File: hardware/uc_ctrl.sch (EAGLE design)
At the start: 32 parts, among them Q4 si2305cd, Q7 si2305cd, T1 BC846, T3 BC846, Y1 32768Hz CFPX-217 12.5pF

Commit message: add pcb
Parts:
- removed C3: 100nF, rcl:C-EUC0805
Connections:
- net N$4 renamed UC_POW
- net 3V_CELL: now also U$9.2; no longer U$9.1
- net GND: no longer C3.1
- net PUSH: now also U$9.1; no longer U$9.2
- net UC_EN: now also U$1.18; no longer U$1.19
- net VCC: no longer C3.2
- net VCC_EN: now also U$1.19; no longer U$1.18
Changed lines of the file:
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@@
 <part name="GND4" library="SparkFun" deviceset="GND" device=""/>
 <part name="GND5" library="SparkFun" deviceset="GND" device=""/>
-<part name="C3" library="rcl" deviceset="C-EU" device="C0805" value="100nF"/>
-<part name="GND6" library="SparkFun" deviceset="GND" device=""/>
 </parts>
 <sheets>
@@
 <instance part="U$5" gate="G$1" x="121.92" y="33.02"/>
 <instance part="SUPPLY1" gate="G$1" x="78.74" y="127"/>
-<instance part="U$9" gate="G$1" x="50.8" y="124.46" rot="R90"/>
+<instance part="U$9" gate="G$1" x="48.26" y="124.46" rot="MR90"/>
 <instance part="D2" gate="G$1" x="71.12" y="119.38"/>
 <instance part="C2" gate="G$1" x="63.5" y="86.36"/>
@@
 <instance part="GND4" gate="1" x="73.66" y="35.56"/>
 <instance part="GND5" gate="1" x="116.84" y="22.86"/>
-<instance part="C3" gate="G$1" x="254" y="121.92" rot="R180"/>
-<instance part="GND6" gate="1" x="254" y="114.3"/>
 </instances>
 <busses>
@@
 </segment>
 <segment>
-<pinref part="C3" gate="G$1" pin="1"/>
-<pinref part="GND6" gate="1" pin="GND"/>
-<wire x1="254" y1="119.38" x2="254" y2="116.84" width="0.1524" layer="91"/>
-</segment>
-<segment>
 <pinref part="C11" gate="G$1" pin="2"/>
 <wire x1="218.44" y1="119.38" x2="220.98" y2="119.38" width="0.1524" layer="91"/>
@@
 <wire x1="269.24" y1="127" x2="269.24" y2="129.54" width="0.1524" layer="91"/>
 <wire x1="269.24" y1="129.54" x2="261.62" y2="129.54" width="0.1524" layer="91"/>
-<pinref part="C3" gate="G$1" pin="2"/>
-<wire x1="261.62" y1="129.54" x2="254" y2="129.54" width="0.1524" layer="91"/>
-<wire x1="254" y1="129.54" x2="254" y2="127" width="0.1524" layer="91"/>
 </segment>
 <segment>
@@
 <net name="UC_EN" class="0">
 <segment>
-<pinref part="U$1" gate="G$1" pin="19"/>
-<wire x1="149.86" y1="86.36" x2="157.48" y2="86.36" width="0.1524" layer="91"/>
-<label x="144.78" y="86.36" size="1.778" layer="95"/>
-</segment>
-<segment>
 <pinref part="R16" gate="G$1" pin="2"/>
 <wire x1="17.78" y1="25.4" x2="22.86" y2="25.4" width="0.1524" layer="91"/>
 <label x="12.7" y="27.94" size="1.778" layer="95"/>
 </segment>
-</net>
-<net name="N$4" class="0">
+<segment>
+<pinref part="U$1" gate="G$1" pin="18"/>
+<wire x1="157.48" y1="88.9" x2="149.86" y2="88.9" width="0.1524" layer="91"/>
+<label x="147.32" y="88.9" size="1.778" layer="95"/>
+</segment>
+</net>
+<net name="UC_POW" class="0">
 <segment>
 <pinref part="Q4" gate="G$1" pin="D"/>
@@
 <wire x1="38.1" y1="106.68" x2="38.1" y2="119.38" width="0.1524" layer="91"/>
 <pinref part="U$8" gate="G$1" pin="3V_CELL"/>
-<pinref part="U$9" gate="G$1" pin="1"/>
 <wire x1="38.1" y1="119.38" x2="38.1" y2="124.46" width="0.1524" layer="91"/>
 <wire x1="38.1" y1="119.38" x2="48.26" y2="119.38" width="0.1524" layer="91"/>
+<junction x="38.1" y="119.38"/>
+<pinref part="U$9" gate="G$1" pin="2"/>
 <wire x1="48.26" y1="119.38" x2="48.26" y2="124.46" width="0.1524" layer="91"/>
-<junction x="38.1" y="119.38"/>
 </segment>
 <segment>
@@
 <net name="VCC_EN" class="0">
 <segment>
-<pinref part="U$1" gate="G$1" pin="18"/>
-<wire x1="149.86" y1="88.9" x2="157.48" y2="88.9" width="0.1524" layer="91"/>
-<label x="144.78" y="88.9" size="1.778" layer="95"/>
-</segment>
-<segment>
 <pinref part="R20" gate="G$1" pin="2"/>
 <wire x1="20.32" y1="83.82" x2="12.7" y2="83.82" width="0.1524" layer="91"/>
 <label x="7.62" y="86.36" size="1.778" layer="95"/>
 </segment>
+<segment>
+<pinref part="U$1" gate="G$1" pin="19"/>
+<wire x1="157.48" y1="86.36" x2="149.86" y2="86.36" width="0.1524" layer="91"/>
+<label x="147.32" y="86.36" size="1.778" layer="95"/>
+</segment>
 </net>
 <net name="PUSH" class="0">
 <segment>
-<pinref part="U$9" gate="G$1" pin="2"/>
-<wire x1="50.8" y1="124.46" x2="50.8" y2="119.38" width="0.1524" layer="91"/>
 <pinref part="D2" gate="G$1" pin="A"/>
 <wire x1="50.8" y1="119.38" x2="63.5" y2="119.38" width="0.1524" layer="91"/>
@@
 <wire x1="68.58" y1="93.98" x2="63.5" y2="93.98" width="0.1524" layer="91"/>
 <junction x="63.5" y="93.98"/>
-</segment>
-</net>
+<pinref part="U$9" gate="G$1" pin="1"/>
+<wire x1="50.8" y1="119.38" x2="50.8" y2="124.46" width="0.1524" layer="91"/>
+</segment>
+</net>

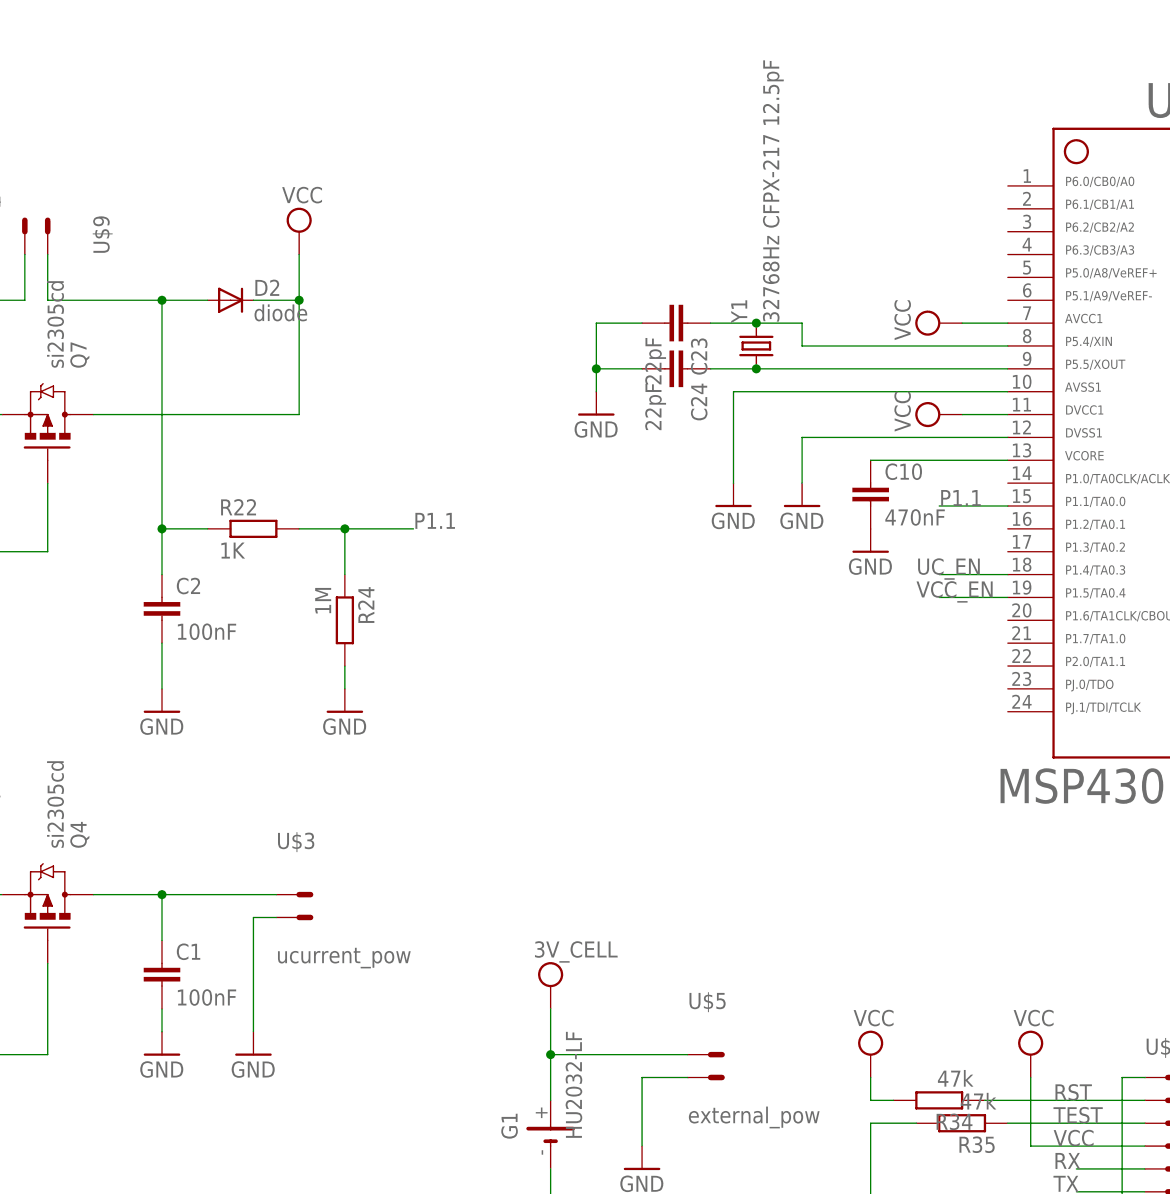
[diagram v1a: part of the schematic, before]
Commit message: also read uCurrent output voltage
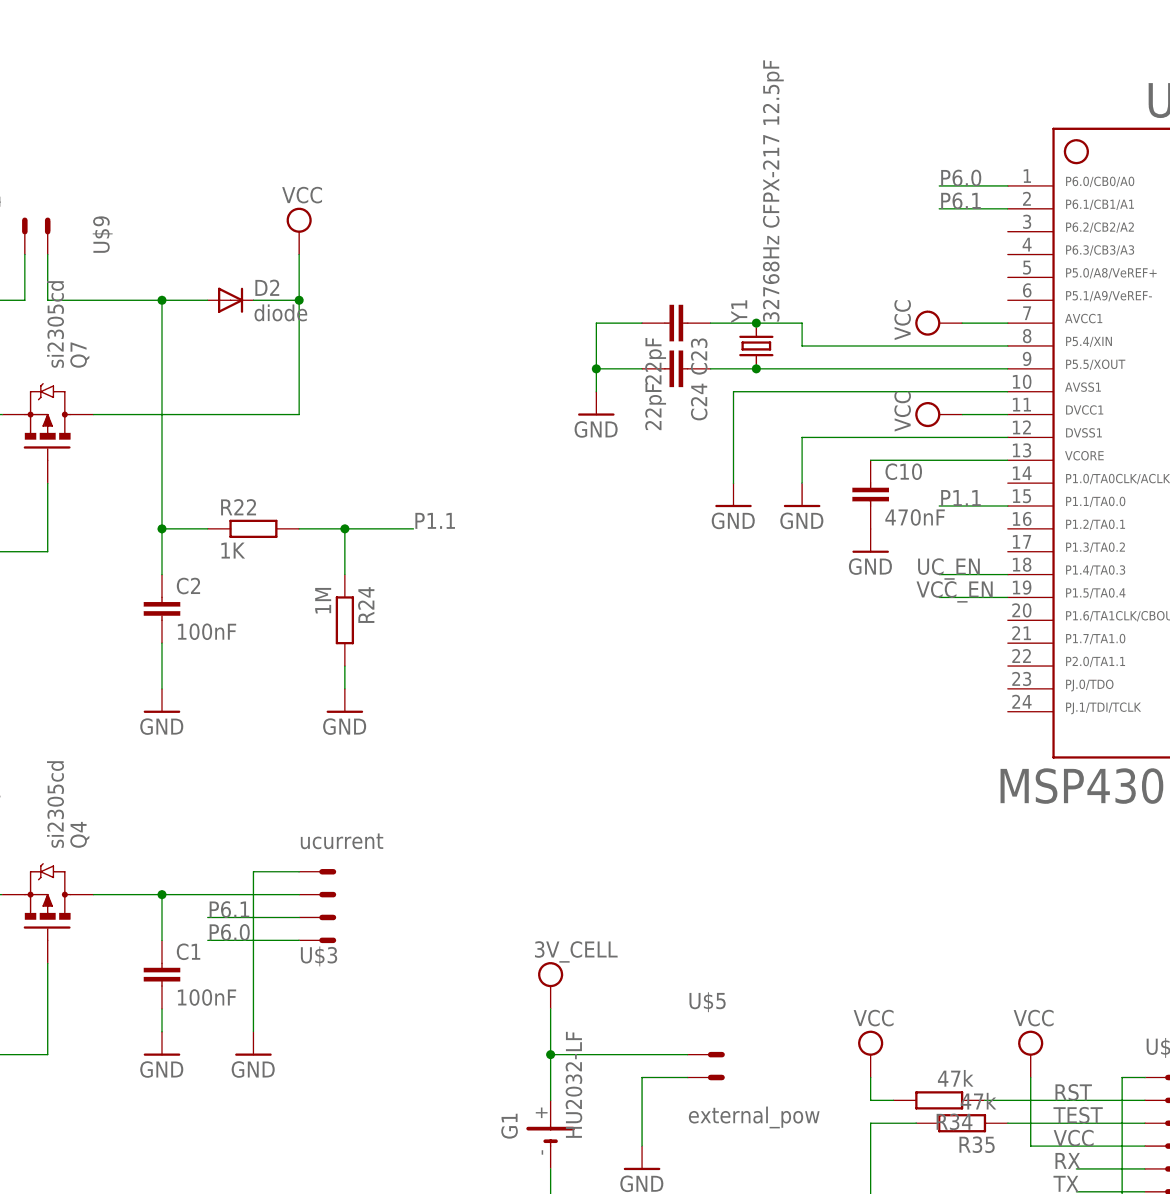
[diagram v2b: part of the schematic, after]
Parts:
- U$3: value ucurrent_pow -> ucurrent; device Simplex-Connectors:MOLEX_2VERTICAL -> Simplex-Connectors:MOLEX_4VERTICAL
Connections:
- new net P6.0: U$1.1, U$3.4
- new net P6.1: U$1.2, U$3.3
- net GND: now also U$3.1; no longer U$3.2
- net UC_POW: now also U$3.2; no longer U$3.1
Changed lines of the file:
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@@
 <part name="U$6" library="Simplex-Power" deviceset="3V_CELL" device=""/>
 <part name="U$8" library="Simplex-Power" deviceset="3V_CELL" device=""/>
-<part name="U$3" library="Simplex-Connectors" deviceset="MOLEX_2" device="VERTICAL" value="ucurrent_pow"/>
 <part name="U$5" library="Simplex-Connectors" deviceset="MOLEX_2" device="VERTICAL" value="external_pow"/>
 <part name="SUPPLY1" library="supply2" deviceset="VCC" device=""/>
@@
 <part name="GND4" library="SparkFun" deviceset="GND" device=""/>
 <part name="GND5" library="SparkFun" deviceset="GND" device=""/>
+<part name="U$3" library="Simplex-Connectors" deviceset="MOLEX_4" device="VERTICAL" value="ucurrent"/>
 </parts>
 <sheets>
@@
 <instance part="U$6" gate="G$1" x="106.68" y="40.64"/>
 <instance part="U$8" gate="G$1" x="38.1" y="124.46"/>
-<instance part="U$3" gate="G$1" x="76.2" y="50.8"/>
 <instance part="U$5" gate="G$1" x="121.92" y="33.02"/>
 <instance part="SUPPLY1" gate="G$1" x="78.74" y="127"/>
@@
 <instance part="GND4" gate="1" x="73.66" y="35.56"/>
 <instance part="GND5" gate="1" x="116.84" y="22.86"/>
+<instance part="U$3" gate="G$1" x="78.74" y="48.26"/>
 </instances>
 <busses>
@@
 </segment>
 <segment>
-<pinref part="U$3" gate="G$1" pin="2"/>
-<wire x1="76.2" y1="50.8" x2="73.66" y2="50.8" width="0.1524" layer="91"/>
-<wire x1="73.66" y1="50.8" x2="73.66" y2="38.1" width="0.1524" layer="91"/>
+<wire x1="73.66" y1="55.88" x2="73.66" y2="38.1" width="0.1524" layer="91"/>
 <pinref part="GND4" gate="1" pin="GND"/>
+<pinref part="U$3" gate="G$1" pin="1"/>
+<wire x1="73.66" y1="55.88" x2="78.74" y2="55.88" width="0.1524" layer="91"/>
 </segment>
 <segment>
@@
 <pinref part="C1" gate="G$1" pin="1"/>
 <wire x1="63.5" y1="53.34" x2="63.5" y2="48.26" width="0.1524" layer="91"/>
-<wire x1="63.5" y1="53.34" x2="76.2" y2="53.34" width="0.1524" layer="91"/>
-<pinref part="U$3" gate="G$1" pin="1"/>
+<wire x1="63.5" y1="53.34" x2="78.74" y2="53.34" width="0.1524" layer="91"/>
 <junction x="63.5" y="53.34"/>
+<pinref part="U$3" gate="G$1" pin="2"/>
 </segment>
 </net>
@@
 </segment>
 </net>
+<net name="P6.1" class="0">
+<segment>
+<pinref part="U$1" gate="G$1" pin="2"/>
+<wire x1="157.48" y1="129.54" x2="149.86" y2="129.54" width="0.1524" layer="91"/>
+<label x="149.86" y="129.54" size="1.778" layer="95"/>
+</segment>
+<segment>
+<pinref part="U$3" gate="G$1" pin="3"/>
+<wire x1="78.74" y1="50.8" x2="68.58" y2="50.8" width="0.1524" layer="91"/>
+<label x="68.58" y="50.8" size="1.778" layer="95"/>
+</segment>
+</net>
+<net name="P6.0" class="0">
+<segment>
+<pinref part="U$1" gate="G$1" pin="1"/>
+<wire x1="157.48" y1="132.08" x2="149.86" y2="132.08" width="0.1524" layer="91"/>
+<label x="149.86" y="132.08" size="1.778" layer="95"/>
+</segment>
+<segment>
+<pinref part="U$3" gate="G$1" pin="4"/>
+<wire x1="78.74" y1="48.26" x2="68.58" y2="48.26" width="0.1524" layer="91"/>
+<label x="68.58" y="48.26" size="1.778" layer="95"/>
+</segment>
+</net>

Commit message: rev 2
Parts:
- removed G1: HU2032-LF, Simplex-Battery:HU2032-LF
- removed U$9: push_button, Simplex-Connectors:MOLEX_2VERTICAL
- added C3, C4, C7: 100nF, rcl:C-EUC0805
- added C5, C6: 10uF, rcl:C-EUC0805
- added LED2: green, led:LEDCHIPLED_0805
- added R2: 100k, rcl:R-EU_R0805W
- added SJ1: (no value), SparkFun-Passives:SOLDERJUMPER_2WAYPASTE1&2
- added SJ2: SOLDERJUMPERNC2, SparkFun-Passives:SOLDERJUMPERNC2
- added U$4: SPST_TACTILE_SW, Simplex-Switches:SPST_TACTILE_SW
- added U$6: MOLEX_2HORIZONTAL, Simplex-Connectors:MOLEX_2HORIZONTAL
- added U1: 3vLDO, SparkFun-PowerIC:V_REG_LDOSMD
- U$2: device Simplex-Connectors:MOLEX_6VERTICAL -> Simplex-Connectors:MOLEX_6HORIZONTAL
- U$3: value ucurrent -> MOLEX_4HORIZONTAL; device Simplex-Connectors:MOLEX_4VERTICAL -> Simplex-Connectors:MOLEX_4HORIZONTAL
- U$5: value external_pow -> sw; device Simplex-Connectors:MOLEX_2VERTICAL -> Simplex-Connectors:MOLEX_2HORIZONTAL
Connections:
- net P6.0 renamed VREF
- net P6.1 renamed VOUT
- removed net 3V_CELL: G1.+, Q4.S, Q7.S, R19.1, R21.1, U$5.1, U$9.2
- removed net P1.1: R22.2, R24.1, U$1.15
- new net N$1: LED2.C, R2.2
- new net N$2: LED2.A, U$1.22
- new net N$4: C6.1, C7.1, D2.C, Q7.D, SJ2.1, U1.EN, U1.IN
- new net N$5: C3.1, U1.BP
- new net N$8: Q4.S, R19.1, SJ1.2
- new net VBAT: R22.2, R24.1, U$1.15, U$1.3
- new net VCC_IN: Q7.S, R21.1, SJ1.3, U$4.1, U$5.2, U$6.2
- net GND: now also C3.2, C4.2, C5.2, C6.2, C7.2, R2.1, U$6.1, U1.GND; no longer G1.-, U$5.2
- net PUSH: now also U$4.2, U$5.1; no longer U$9.1
- net UC_EN: now also U$1.19; no longer U$1.18
- net VCC: now also C4.1, C5.1, SJ1.1, SJ2.2, U1.OUT; no longer D2.C, Q7.D
- net VCC_EN: now also U$1.18; no longer U$1.19
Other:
- note added: "jumper settings: if Vcc_in is between 2.8-3.0 V SJ1 - short open SJ2 - short if Vcc_in is between 3.1-5.0V SJ1 - open short SJ2 - open"
- moved on the sheet: C1, C10, C11, C2, C23, C24, C8, C9, D2, Q4, Q7, R16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
